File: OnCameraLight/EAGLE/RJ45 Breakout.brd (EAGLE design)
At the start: 33.7 x 35.5 mm, 7 parts, among them J1 RJHSE-5381

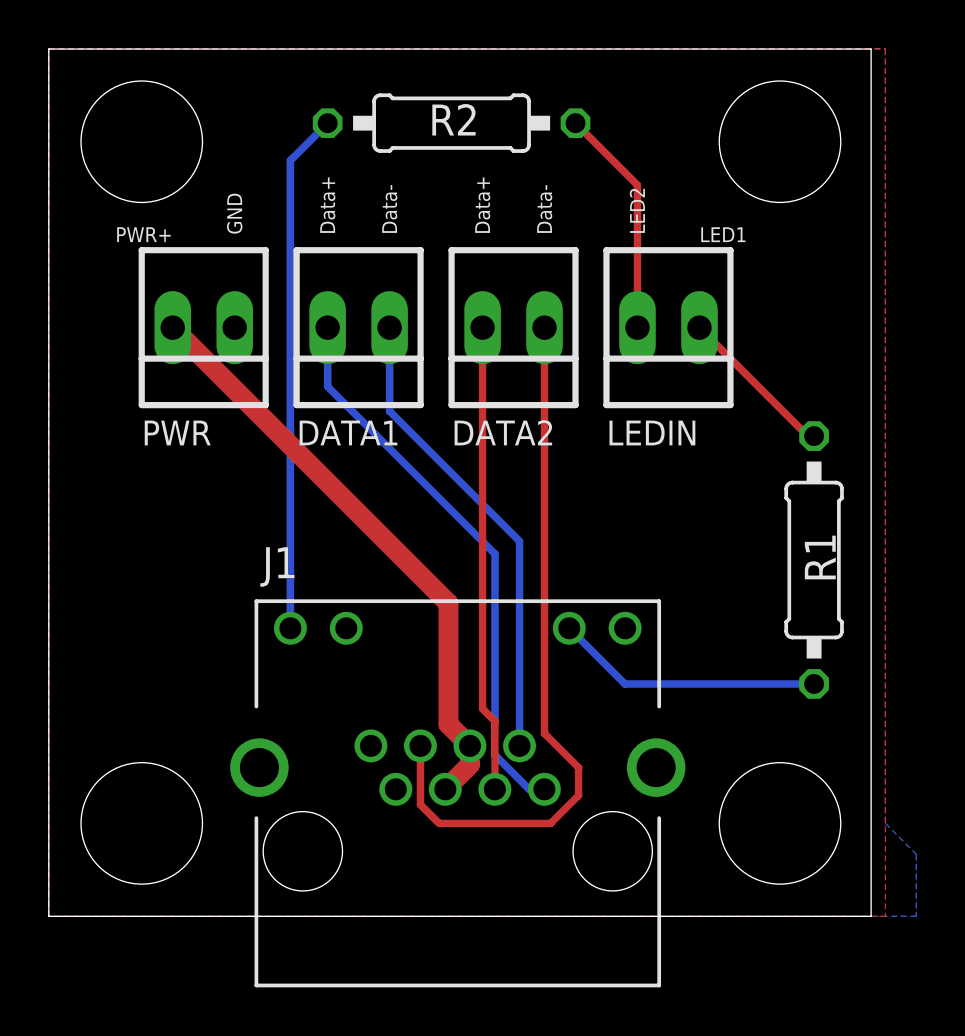
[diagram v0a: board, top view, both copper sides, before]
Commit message: Slim down some spacings to possibly use some 8 pin headers instead of 4x 2pin.  Fix hole drill sizes.
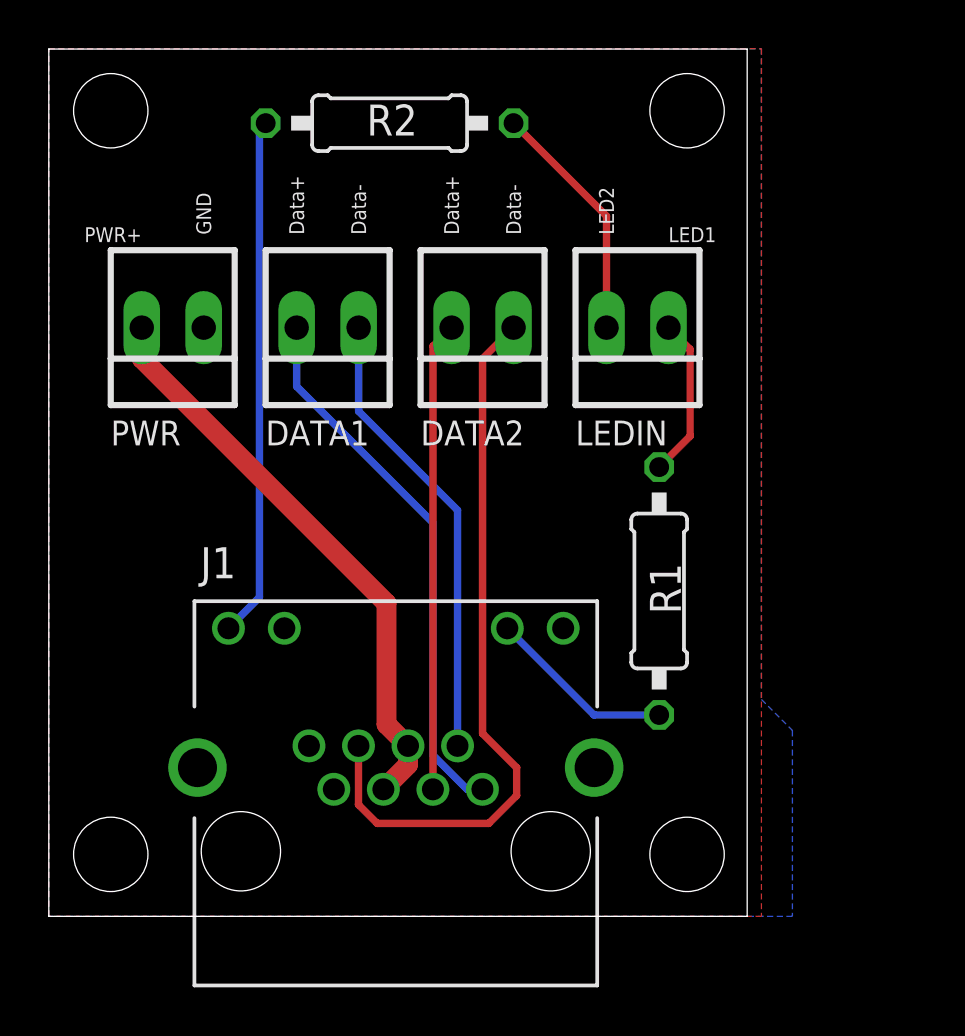
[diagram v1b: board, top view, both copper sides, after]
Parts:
- moved R1 6.48 mm to (25.0, 13.3)
- moved R2 2.54 mm to (14.0, 32.5)
- moved J1 2.54 mm to (14.2, 2.67)
- moved DATA1 1.27 mm to (11.4, 24.1)
- moved DATA2 1.27 mm to (17.8, 24.1)
- moved LEDIN 1.27 mm to (24.1, 24.1)
- moved PWR 1.27 mm to (5.08, 24.1)
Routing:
- net LED1: track 11.0 -> 7.70 mm
- net VCC: track 24.4 -> 23.9 mm
- net LED2IN: track 9.43 -> 9.96 mm
- net DATA2-: track 29.4 -> 30.0 mm
- net DATA1-: track 19.3 -> 18.8 mm
- net DATA1+: track 23.0 -> 22.4 mm
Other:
- board size 33.7 x 35.5 mm -> 28.6 x 35.5 mm

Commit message: Go through and fix notation on RS485 wiring everywhere to use the standard A/B notation.
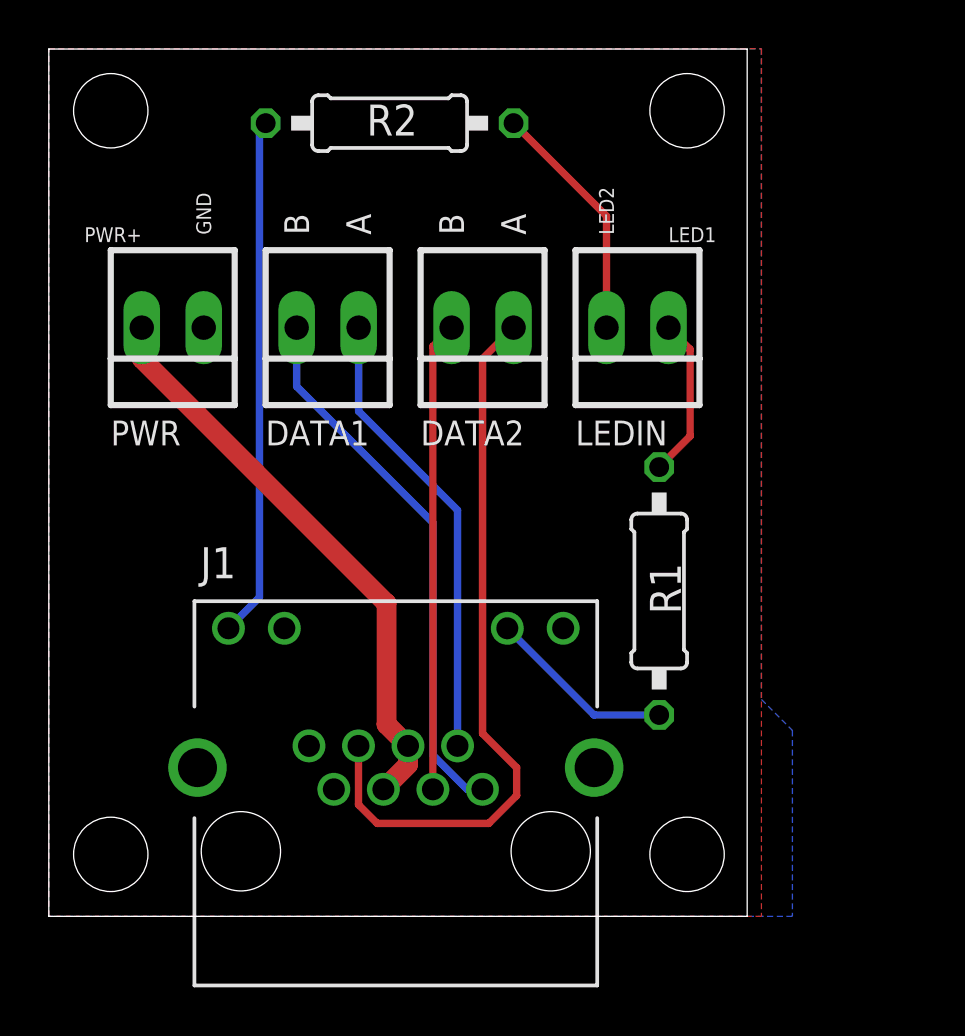
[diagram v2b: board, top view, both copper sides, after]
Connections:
- net DATA1+ renamed DATA1B
- net DATA1- renamed DATA1A
- net DATA2+ renamed DATA2B
- net DATA2- renamed DATA2A
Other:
- board text added: "A"
- board text added: "B"
- board text removed: "Data+"
- board text removed: "Data-"
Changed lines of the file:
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@@
 <text x="3.81" y="27.94" size="0.6096" layer="25" rot="R180" align="center-left">PWR+</text>
 <text x="6.35" y="27.94" size="0.6096" layer="25" rot="R90" align="center-left">GND</text>
-<text x="10.16" y="27.94" size="0.6096" layer="25" rot="R90" align="center-left">Data+</text>
-<text x="12.7" y="27.94" size="0.6096" layer="25" rot="R90" align="center-left">Data-</text>
+<text x="10.16" y="27.94" size="1.016" layer="25" rot="R90" align="center-left">B</text>
+<text x="12.7" y="27.94" size="1.016" layer="25" rot="R90" align="center-left">A</text>
 <text x="22.86" y="27.94" size="0.6096" layer="25" rot="R90" align="center-left">LED2</text>
 <text x="25.4" y="27.94" size="0.6096" layer="25" align="center-left">LED1</text>
@@
 <text x="22.987" y="17.907" size="1.4224" layer="26" rot="MR0">RS485 + Power
 Breakout</text>
-<text x="16.51" y="27.94" size="0.6096" layer="25" rot="R90" align="center-left">Data+</text>
-<text x="19.05" y="27.94" size="0.6096" layer="25" rot="R90" align="center-left">Data-</text>
+<text x="16.51" y="27.94" size="1.016" layer="25" rot="R90" align="center-left">B</text>
+<text x="19.05" y="27.94" size="1.016" layer="25" rot="R90" align="center-left">A</text>
 </plain>
 <attributes>
@@
 <wire x1="22.86" y1="28.702" x2="22.86" y2="24.13" width="0.3048" layer="1"/>
 </signal>
-<signal name="DATA2-">
-<contactref element="DATA2" pad="1"/>
-<contactref element="J1" pad="6"/>
-<wire x1="19.05" y1="24.13" x2="17.78" y2="22.86" width="0.3048" layer="1"/>
-<wire x1="17.78" y1="22.86" x2="17.78" y2="7.493" width="0.3048" layer="1"/>
-<wire x1="19.177" y1="6.096" x2="19.177" y2="4.953" width="0.3048" layer="1"/>
-<wire x1="18.034" y1="3.81" x2="19.177" y2="4.953" width="0.3048" layer="1"/>
-<wire x1="12.694" y1="4.578" x2="13.462" y2="3.81" width="0.3048" layer="1"/>
-<wire x1="12.694" y1="4.578" x2="12.694" y2="6.987" width="0.3048" layer="1"/>
-<wire x1="17.78" y1="7.493" x2="19.177" y2="6.096" width="0.3048" layer="1"/>
-<wire x1="13.462" y1="3.81" x2="18.034" y2="3.81" width="0.3048" layer="1"/>
-</signal>
-<signal name="DATA1+">
-<contactref element="DATA1" pad="2"/>
-<contactref element="J1" pad="1"/>
-<wire x1="10.16" y1="24.13" x2="10.16" y2="21.717" width="0.3048" layer="16"/>
-<wire x1="15.748" y1="6.60735" x2="17.14835" y2="5.207" width="0.3048" layer="16"/>
-<wire x1="17.14835" y1="5.207" x2="17.774" y2="5.207" width="0.3048" layer="16"/>
-<wire x1="10.16" y1="21.717" x2="15.748" y2="16.129" width="0.3048" layer="16"/>
-<wire x1="15.748" y1="16.129" x2="15.748" y2="6.60735" width="0.3048" layer="16"/>
-</signal>
-<signal name="DATA2+">
-<contactref element="DATA2" pad="2"/>
-<contactref element="J1" pad="3"/>
-<wire x1="16.51" y1="24.13" x2="15.748" y2="23.368" width="0.3048" layer="1"/>
-<wire x1="15.748" y1="23.368" x2="15.748" y2="5.211" width="0.3048" layer="1"/>
-<wire x1="15.748" y1="5.211" x2="15.744" y2="5.207" width="0.3048" layer="1"/>
-</signal>
-<signal name="DATA1-">
-<contactref element="DATA1" pad="1"/>
-<contactref element="J1" pad="2"/>
-<wire x1="12.7" y1="24.13" x2="12.7" y2="20.701" width="0.3048" layer="16"/>
-<wire x1="16.754" y1="16.647" x2="16.754" y2="6.987" width="0.3048" layer="16"/>
-<wire x1="12.7" y1="20.701" x2="16.754" y2="16.647" width="0.3048" layer="16"/>
-</signal>
 <signal name="VCC">
 <contactref element="J1" pad="4"/>
@@
 <wire x1="22.346" y1="8.255" x2="18.794" y2="11.807" width="0.3048" layer="16"/>
 </signal>
+<signal name="DATA1B">
+<contactref element="J1" pad="1"/>
+<contactref element="DATA1" pad="2"/>
+<wire x1="10.16" y1="24.13" x2="10.16" y2="21.717" width="0.3048" layer="16"/>
+<wire x1="17.14835" y1="5.207" x2="15.748" y2="6.60735" width="0.3048" layer="16"/>
+<wire x1="10.16" y1="21.717" x2="15.748" y2="16.129" width="0.3048" layer="16"/>
+<wire x1="15.748" y1="16.129" x2="15.748" y2="6.60735" width="0.3048" layer="16"/>
+<wire x1="17.774" y1="5.207" x2="17.14835" y2="5.207" width="0.3048" layer="16"/>
+</signal>
+<signal name="DATA1A">
+<contactref element="J1" pad="2"/>
+<contactref element="DATA1" pad="1"/>
+<wire x1="12.7" y1="24.13" x2="12.7" y2="20.701" width="0.3048" layer="16"/>
+<wire x1="16.754" y1="16.647" x2="12.7" y2="20.701" width="0.3048" layer="16"/>
+<wire x1="16.754" y1="6.987" x2="16.754" y2="16.647" width="0.3048" layer="16"/>
+</signal>
+<signal name="DATA2B">
+<contactref element="J1" pad="3"/>
+<contactref element="DATA2" pad="2"/>
+<wire x1="15.744" y1="5.207" x2="15.744" y2="23.364" width="0.3048" layer="1"/>
+<wire x1="15.744" y1="23.364" x2="16.51" y2="24.13" width="0.3048" layer="1"/>
+</signal>
+<signal name="DATA2A">
+<contactref element="J1" pad="6"/>
+<contactref element="DATA2" pad="1"/>
+<wire x1="19.05" y1="24.13" x2="17.78" y2="22.86" width="0.3048" layer="1"/>
+<wire x1="17.78" y1="22.86" x2="17.78" y2="7.493" width="0.3048" layer="1"/>
+<wire x1="19.177" y1="6.096" x2="19.177" y2="4.953" width="0.3048" layer="1"/>
+<wire x1="18.034" y1="3.81" x2="19.177" y2="4.953" width="0.3048" layer="1"/>
+<wire x1="12.694" y1="4.578" x2="13.462" y2="3.81" width="0.3048" layer="1"/>
+<wire x1="17.78" y1="7.493" x2="19.177" y2="6.096" width="0.3048" layer="1"/>
+<wire x1="13.462" y1="3.81" x2="18.034" y2="3.81" width="0.3048" layer="1"/>
+<wire x1="12.694" y1="6.987" x2="12.694" y2="4.578" width="0.3048" layer="1"/>
+</signal>
 </signals>
